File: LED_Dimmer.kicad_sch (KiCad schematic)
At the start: 19 parts, among them J1 2.54mm Header, J2 2.54mm Header, Q1 PJA3404A_R1_00001, U1 TLC555CDR

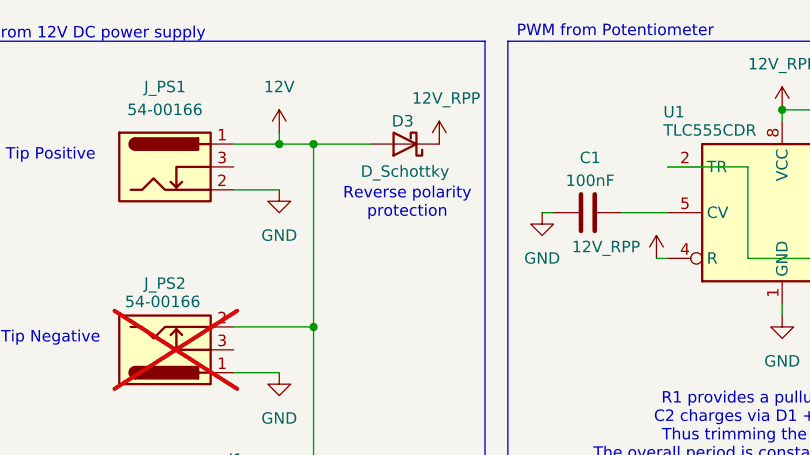
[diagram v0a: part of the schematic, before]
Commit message: Add Schottky part number
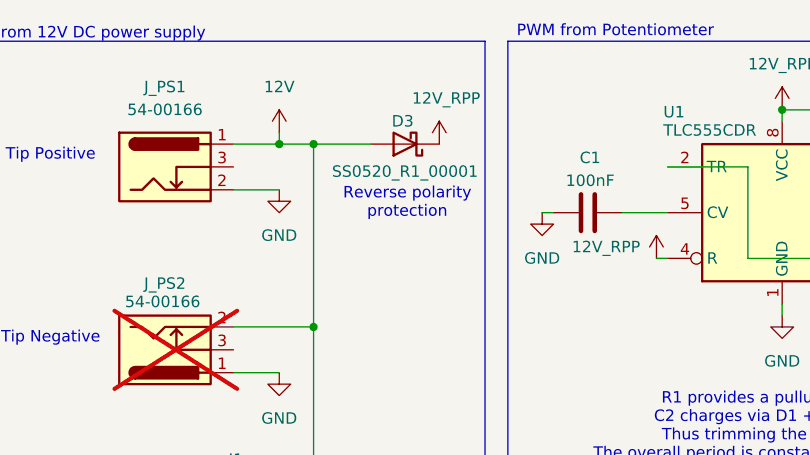
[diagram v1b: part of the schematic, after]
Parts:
- D3: value D_Schottky -> SS0520_R1_00001
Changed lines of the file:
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@@
 			)
 		)
-		(property "Value" "D_Schottky"
+		(property "Value" "SS0520_R1_00001"
 			(at 80.01 90.678 0)
 			(effects

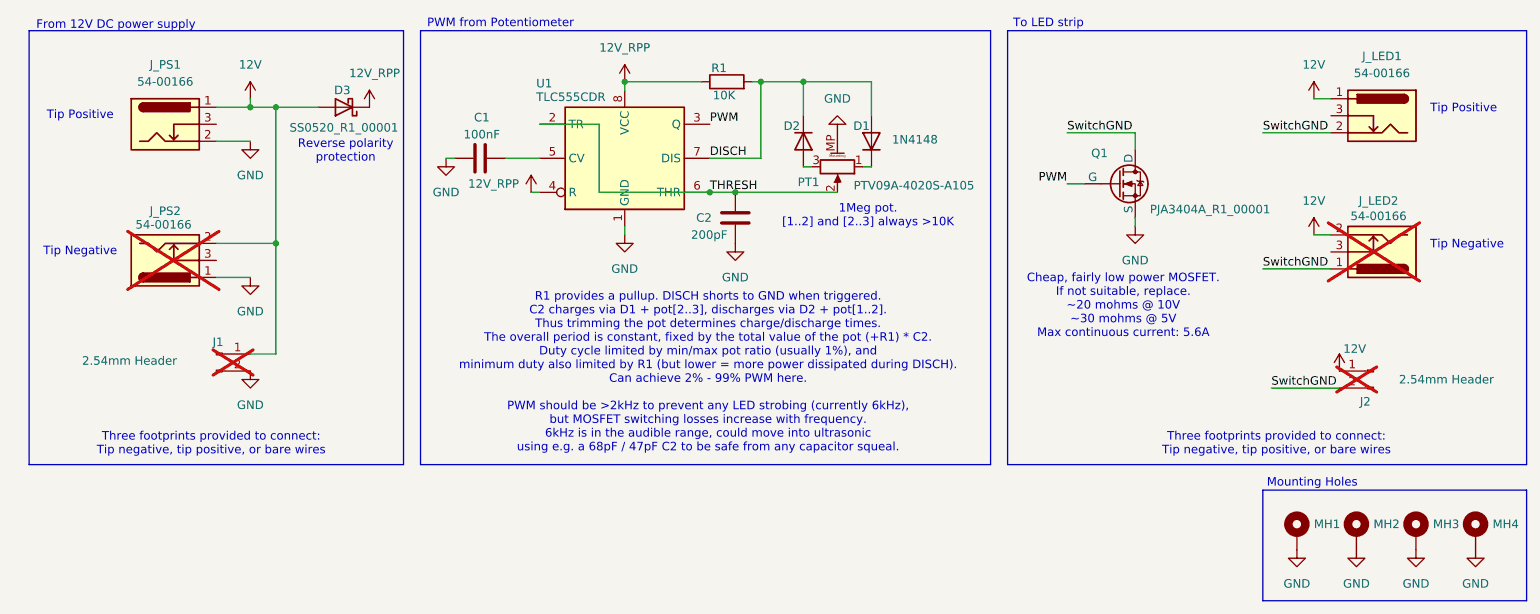
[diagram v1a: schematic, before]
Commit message: Tidy schematic, add serial number location to PCB
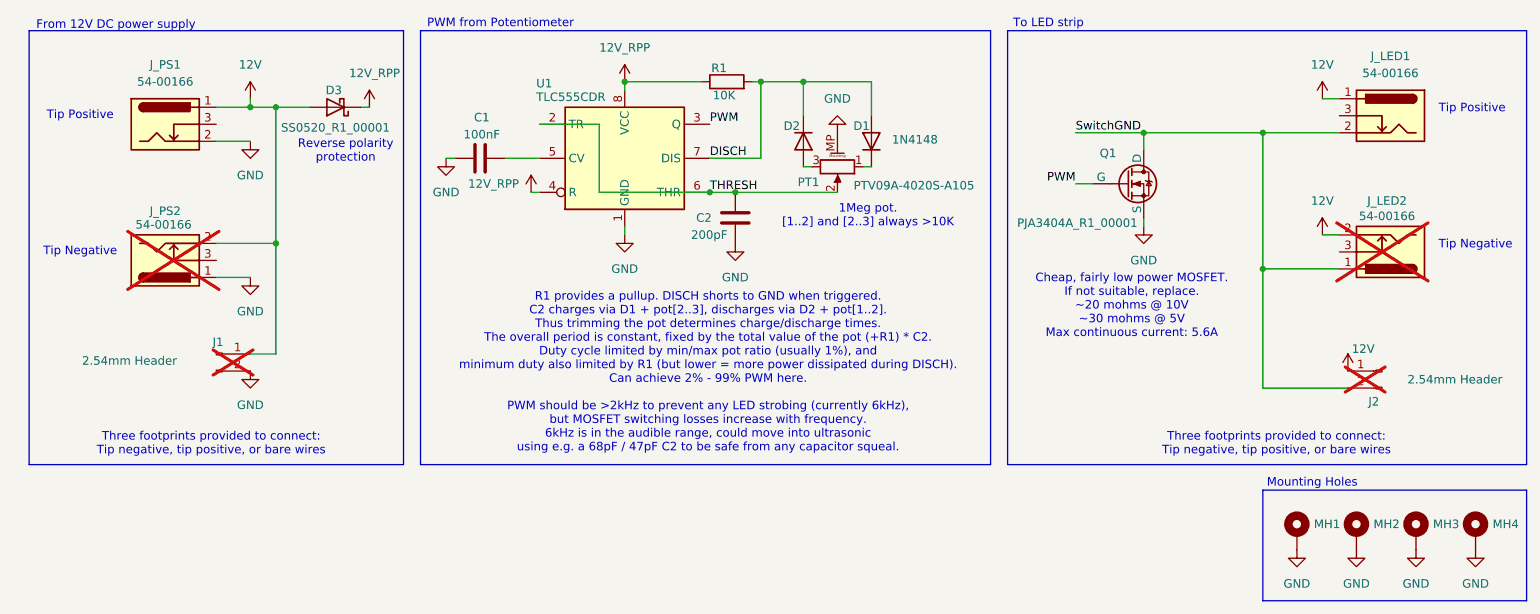
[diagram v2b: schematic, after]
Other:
- moved on the sheet: D3, J2, J_LED1, J_LED2, Q1
